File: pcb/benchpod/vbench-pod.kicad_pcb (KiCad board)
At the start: 4 copper layers, 100 x 80 mm, 505 parts, among them J1 Conn_02x10_Odd_Even, J4 Screw_Terminal_01x02, J5 Screw_Terminal_01x02, J6 Screw_Terminal_01x02, J7 HR911105A_C12074, J8 Screw_Terminal_01x02, J9 Screw_Terminal_01x02, K1 G6K-2F-Y DC5, K2 G6K-2F-Y DC5, K3 G6K-2F-Y DC5, K4 G6K-2F-Y DC5, Q1 BCP56, SW1 TS-1088-AR02016, SW2 TS-1088-AR02016, U1 ICE40UP5K-SG48ITR, U10 TCAN1044VDRBRQ1, U18 SN74LVC2G66DCUR, U19 SN74LVC2G66DCUR, U2 W25Q64JVSSIQ, U20 SN74LVC2G66DCUR, U21 SN74LVC2G66DCUR, U22 SRV05-4.TCT, U23 SRV05-4.TCT, U24 SN74LVC2G66DCUR, U25 SRV05-4.TCT, U26 TPS259470ARPWR, U27 TPS259470ARPWR, U29 INA238AIDGSR, U3 TPS7A2050PDBVR, U30 TPS82130SILR, U31 AP2112K-1.2, U32 AP2112K-2.5TRG1, U33 INA238AIDGSR, U34 SRV05-4.TCT, U36 MCP33131D-10-E/MS, U37 THS4551IDGKR, U38 ADR4540BRZ-R7, U39 AP2112K-1.8TRG1, U4 ESP32-C3-MINI-1-N4, U40 OPA810IDBVR, U41 LM27761DSGR, U42 LM7705MM/NOPB, U43 DAC8551IADGKR, U44 OPA2365AIDR, U45 OPA2992IDR, U46 AP2112K-3.3, U47 TMUX1104DGSR, U48 TMUX1104DGSR, U49 TPS65131TRGERQ1, U5 STM32H563ZIT6, U50 TPS7A1901DRBR, U51 OPA2992IDR, U52 AP2112K-1.8TRG1, U53 TPL7407LAPWR, U54 TCA9554PWR, U55 TCA9554PWR, U56 TCA9554PWR, U57 TPS259470ARPWR, U58 TCA9554PWR, U6 LAN8742AI-CZ-TR, U7 APS6404L-3SQR-SN_C5333729, U8 TPS2116DRLR, U9 XTR116UA/2K5, X1 SX3M48.000B10F20TNN, Y1 Crystal_GND24, Y2 Crystal_GND24

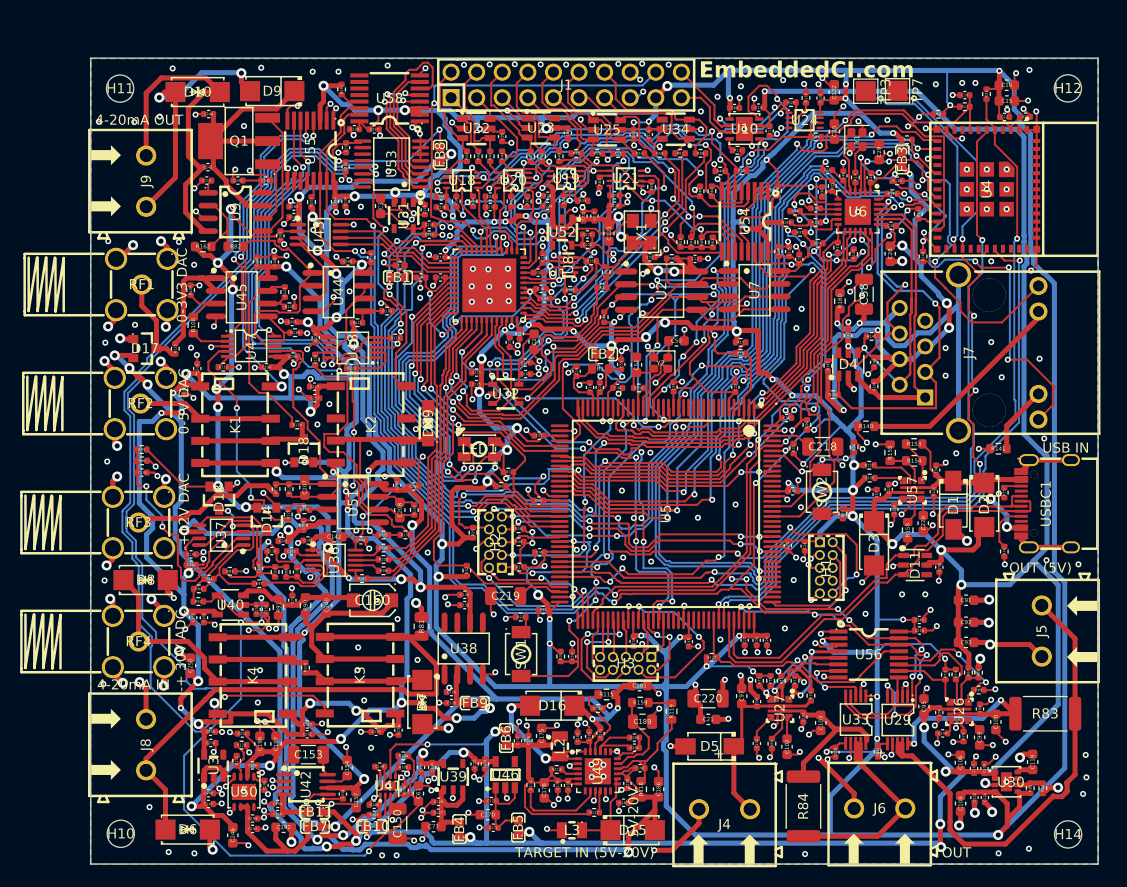
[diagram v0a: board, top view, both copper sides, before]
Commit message: txp/txn/rxp/rxn rerouting
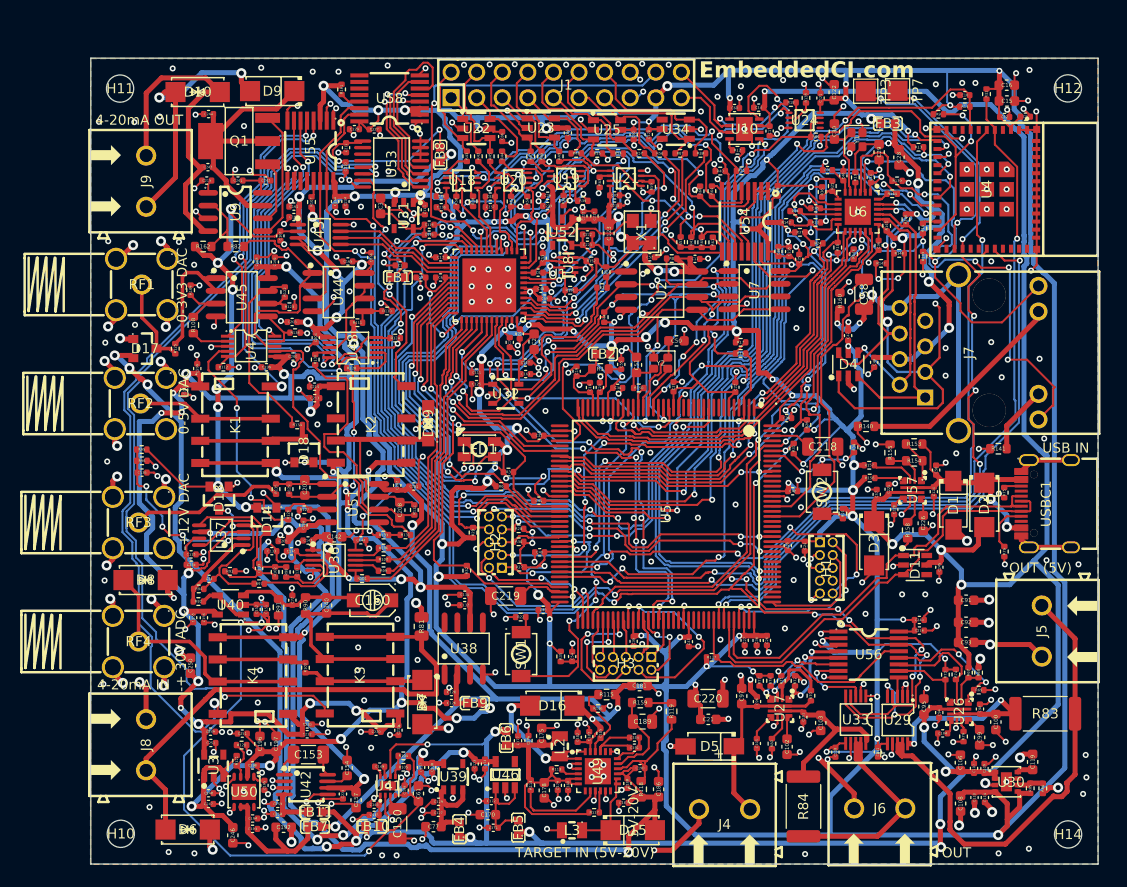
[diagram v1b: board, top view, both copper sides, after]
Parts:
- moved R146 16.9 mm to (119.9, 36.1)
- moved R148 15.5 mm to (119.3, 39.5), turned to 180 degrees
- moved R147 11.5 mm to (117.5, 40.5), turned to 0 degrees
- moved R145 11.1 mm to (118.0, 36.8), turned to 90 degrees
- moved C28 9.61 mm to (119.2, 30.0)
- moved FB3 3.84 mm to (118.2, 26.6), turned to 0 degrees
- moved C35 2.29 mm to (117.2, 38.7), turned to -90 degrees
- moved R10 1.52 mm to (121.6, 37.0), turned to 90 degrees
- moved R13 1.36 mm to (121.2, 29.0)
- turned R149 to -90 degrees
- turned R9 to 0 degrees
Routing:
- net /Ethernet/RXP: track 39.7 -> 48.7 mm, vias 2 -> 4
- net /Ethernet/CHSGND: track 41.4 -> 33.5 mm, vias 2 -> 3
- net 2.05V: track 23.7 -> 17.8 mm, vias 2 -> 4
- net /ESP32_BOOT: track 86.7 -> 92.3 mm
- net −0V232: track 51.7 -> 47.9 mm
- net /ESP32_CTS: track 76.2 -> 79.4 mm
- net /Ethernet/TXN: track 28.4 -> 25.3 mm
- net /ESP32_DATAREADY: track 68.5 -> 71.5 mm
- net /ESP32_CS: track 72.5 -> 74.7 mm, vias 2 -> 3
- net Net-(U4-IO18): track 20.7 -> 22.8 mm
- net /Ethernet/GREEN_LED: track 48.9 -> 50.8 mm, vias 6 -> 4
- net /Ethernet/TXP: track 30.8 -> 29.0 mm
- net /analog to digital v2/AMP_MEASURE_IN: track 57.3 -> 55.7 mm
- net /Ethernet/RXN: track 27.2 -> 26.2 mm
- net /Ethernet/VDDA: track 63.9 -> 64.8 mm, vias 6 -> 10
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
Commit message: nrst control
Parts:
- added R7: 10k, Resistor_SMD:R_0402_1005Metric, F.Cu at (103.3, 22.6)
- J1: value Conn_02x10_Odd_Even -> PZ254V-12-22P; footprint lcsc:HDR-TH_20P-P2.54-V-M-R2-C10-S2.54 -> lcsc_footprints:C492428_HDR-TH_22P-P2_54-V-M-R2-C11-S2_54
- moved J1 1.54 mm to (87.8, 22.7)
- moved C17 0.78 mm to (106.5, 26.6)
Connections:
- U5 pad 14: unconnected-(U5-PF4-Pad14) -> /NRST_CONTROL
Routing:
- net /NRST_CONTROL: track 0.00 -> 54.3 mm, vias 0 -> 2
- net LA_VCCIO: track 33.8 -> 75.3 mm, vias 8 -> 11
- net /Ethernet/RXP: track 48.7 -> 41.1 mm, vias 4 -> 3
- net GND: track 517.5 -> 510.8 mm, vias 492 -> 473
- net +3V3: track 895.1 -> 897.2 mm
- net /LA_OUT2: track 12.3 -> 13.8 mm
- net /analog switching/+5V_COM: track 19.0 -> 17.7 mm
- net /FDCAN1_RX: track 72.2 -> 73.3 mm
- net /LA_INPUT5: track 6.58 -> 7.51 mm
- net /CAN+: track 16.5 -> 15.6 mm
- net /FDCAN1_TX: track 58.2 -> 59.0 mm
- net +5V: track 263.5 -> 262.9 mm
- net /I2C1_SDA: track 31.1 -> 30.5 mm
- net /CAN_TERM_CTRL: track 56.9 -> 56.3 mm
- net /I2C1_SCL: track 41.6 -> 41.1 mm
